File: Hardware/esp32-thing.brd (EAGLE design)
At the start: 25.4 x 58.9 mm, 72 parts, among them Q1 2.5A/30V, Q2 MBT3904DW1T1, U1 MCP73831, U2 ESP3212, U3 AP2112K-3.3V, U4 FT231XS, U5 W25Q32FVSS, Y1 26MHz, Y2 32.768kHz

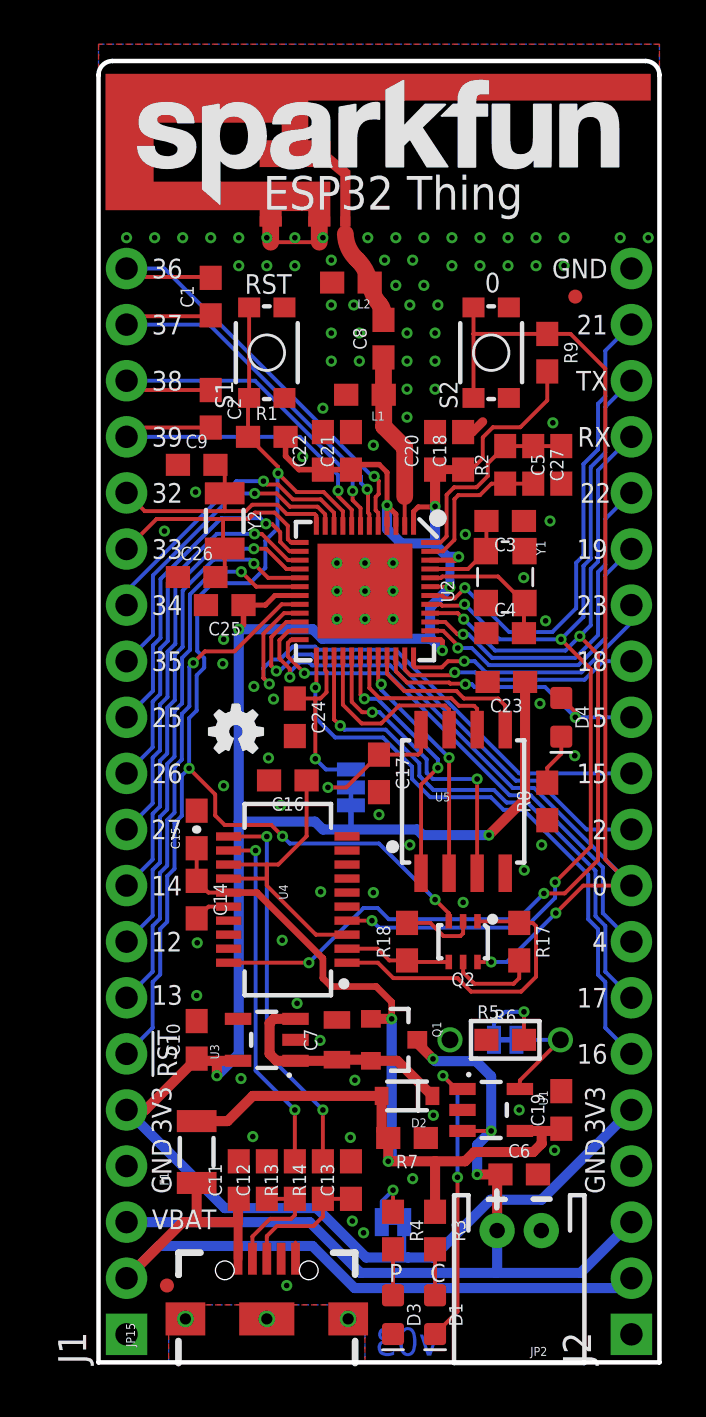
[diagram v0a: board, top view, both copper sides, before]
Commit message: Upping to v10, fixing some silk.
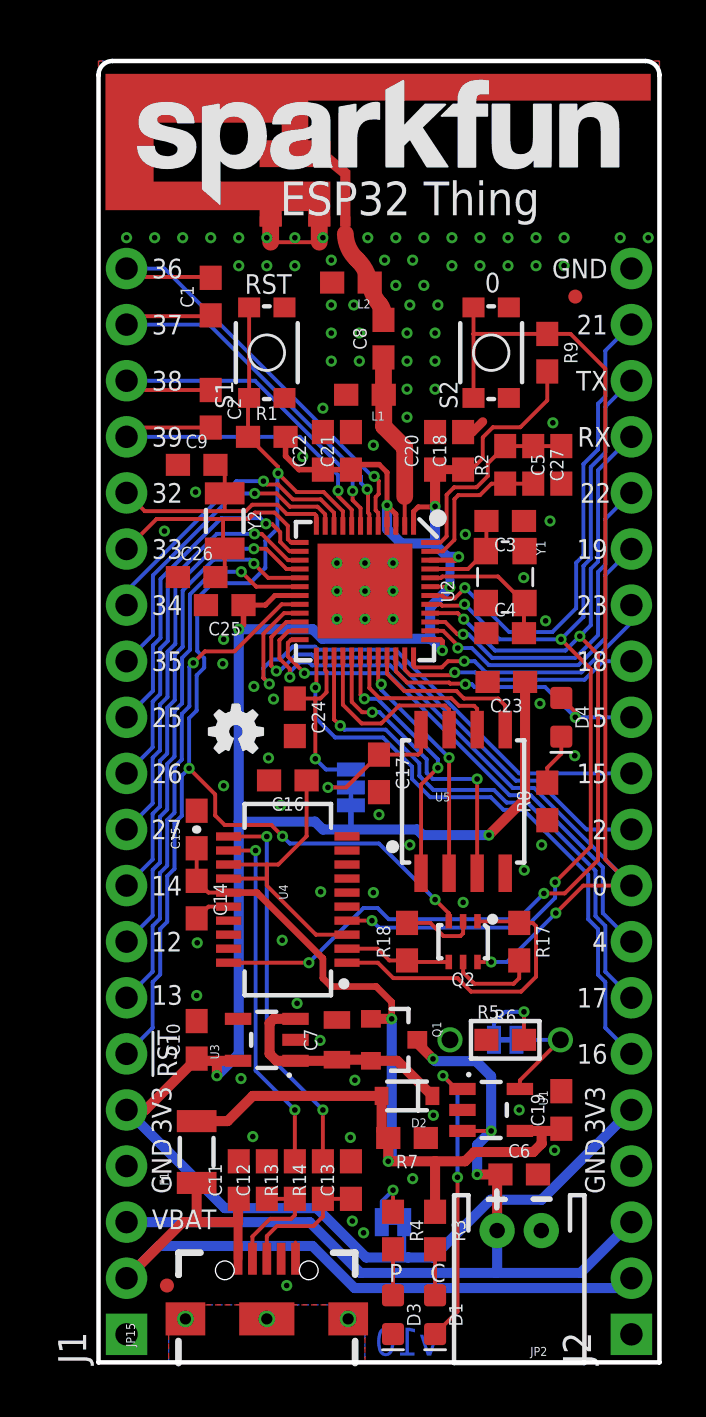
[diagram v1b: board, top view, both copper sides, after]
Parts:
- moved LOGO3 0.13 mm to (23.7, 53.1)
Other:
- board text added: "http://sfe.io/t5O7"
- board text added: "v10"
- board text removed: "http://sfe.io/t507"
- board text removed: "v03"
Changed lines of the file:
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@@
 <?xml version="1.0" encoding="utf-8"?>
 <!DOCTYPE eagle SYSTEM "eagle.dtd">
-<eagle version="7.6.0">
+<eagle version="7.5.0">
 <drawing>
 <settings>
@@
 <layer number="47" name="Measures" color="7" fill="1" visible="no" active="yes"/>
 <layer number="48" name="Document" color="7" fill="1" visible="no" active="yes"/>
-<layer number="49" name="Reference" color="7" fill="1" visible="no" active="yes"/>
+<layer number="49" name="Reference" color="7" fill="1" visible="yes" active="yes"/>
 <layer number="50" name="dxf" color="7" fill="1" visible="no" active="no"/>
 <layer number="51" name="tDocu" color="6" fill="1" visible="yes" active="yes"/>
@@
 <text x="17.8435" y="48.4505" size="0.889" layer="21" font="vector" ratio="15" align="bottom-center">0</text>
 <text x="22.9235" y="6.35" size="0.8128" layer="22" font="vector" ratio="15" rot="MR270" align="bottom-center">VBAT</text>
-<text x="13.335" y="53.721" size="1.524" layer="21" font="vector" ratio="15" align="top-center">ESP32 Thing</text>
+<text x="14.097" y="53.467" size="1.524" layer="21" font="vector" ratio="15" align="top-center">ESP32 Thing</text>
 <dimension x1="0" y1="0" x2="0" y2="58.928" x3="-5.08" y3="29.464" textsize="1.778" textratio="15" layer="47" dtype="vertical" width="0.127" unit="inch" precision="3"/>
 <dimension x1="0" y1="0" x2="25.4" y2="0" x3="12.7" y3="-7.62" textsize="1.778" textratio="15" layer="47" dtype="horizontal" width="0.127" unit="inch" precision="3"/>
@@
 PROG</text>
 <text x="12.573" y="26.162" size="0.8128" layer="22" font="vector" ratio="15" rot="MR270" align="top-center">SJ3</text>
-<text x="13.97" y="0.3048" size="1.27" layer="16" font="vector" ratio="15" rot="MR0" align="bottom-center">v03</text>
+<text x="13.97" y="0.3048" size="1.27" layer="16" font="vector" ratio="15" rot="MR0" align="bottom-center">v10</text>
 <text x="13.97" y="-19.05" size="1.778" layer="51" font="vector" ratio="15">Jim Lindblom</text>
 <text x="13.462" y="3.6449" size="0.8128" layer="21" font="vector" ratio="15" align="bottom-center">P</text>
 <text x="15.367" y="3.6449" size="0.8128" layer="21" font="vector" ratio="15" align="bottom-center">C</text>
-<text x="12.065" y="54.61" size="1.27" layer="22" font="vector" ratio="15" rot="MR0" align="top-center">ESP32 Thing</text>
+<text x="12.065" y="54.61" size="1.524" layer="22" font="vector" ratio="15" rot="MR0" align="top-center">ESP32 Thing</text>
 <wire x1="18.034" y1="6.9977" x2="18.034" y2="7.7597" width="0.254" layer="21"/>
 <wire x1="18.415" y1="7.3787" x2="17.653" y2="7.3787" width="0.254" layer="21"/>
@@
 <text x="11.43" y="27.686" size="0.8128" layer="22" font="vector" ratio="15" rot="MR90" align="center-left">FLASH
 VCC</text>
-<text x="12.065" y="52.07" size="1.27" layer="22" font="vector" ratio="15" rot="MR0" align="center">http://sfe.io/t507</text>
+<text x="12.446" y="51.816" size="1.397" layer="22" font="vector" ratio="15" rot="MR0" align="center">http://sfe.io/t5O7</text>
 <text x="2.413" y="41.91" size="0.889" layer="21" font="vector" ratio="15" align="center-left">39</text>
 <text x="2.413" y="44.45" size="0.889" layer="21" font="vector" ratio="15" align="center-left">38</text>
@@
 <element name="FD1" library="SparkFun-Aesthetics" package="MICRO-FIDUCIAL" value="FIDUCIALUFIDUCIAL" x="3.0988" y="3.4798"/>
 <element name="FD2" library="SparkFun-Aesthetics" package="MICRO-FIDUCIAL" value="FIDUCIALUFIDUCIAL" x="21.59" y="48.26"/>
-<element name="LOGO3" library="SparkFun-Aesthetics" package="SFE_LOGO_NAME_.2" value="SFE_LOGO_NAME.2_INCH" x="23.749" y="53.213" rot="MR0"/>
+<element name="LOGO3" library="SparkFun-Aesthetics" package="SFE_LOGO_NAME_.2" value="SFE_LOGO_NAME.2_INCH" x="23.749" y="53.086" rot="MR0"/>
 <element name="R9" library="SparkFun-Resistors" package="0603" value="10k" x="20.32" y="45.72" rot="R270">
 <attribute name="PROD_ID" value="RES-00824" x="20.32" y="45.72" size="1.778" layer="27" font="vector" ratio="15" rot="R270" display="off"/>
@@
 <contactref element="C25" pad="2"/>
 <polygon width="0.1778" layer="1" isolate="0.1778" rank="6">
-<vertex x="0" y="59.69"/>
+<vertex x="0" y="58.928"/>
 <vertex x="0" y="0"/>
 <vertex x="25.4" y="0"/>
-<vertex x="25.4" y="59.69"/>
+<vertex x="25.4" y="58.928"/>
 </polygon>
 <polygon width="0.1778" layer="16" isolate="0.1778" rank="6">
-<vertex x="25.4" y="59.69"/>
+<vertex x="25.4" y="58.928"/>
 <vertex x="25.4" y="0"/>
 <vertex x="0" y="0"/>
-<vertex x="0" y="59.69"/>
+<vertex x="0" y="58.928"/>
 </polygon>
 <contactref element="S1" pad="2"/>

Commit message: Fixing label, SJ3 silk, reinforcing connection on USB ground.
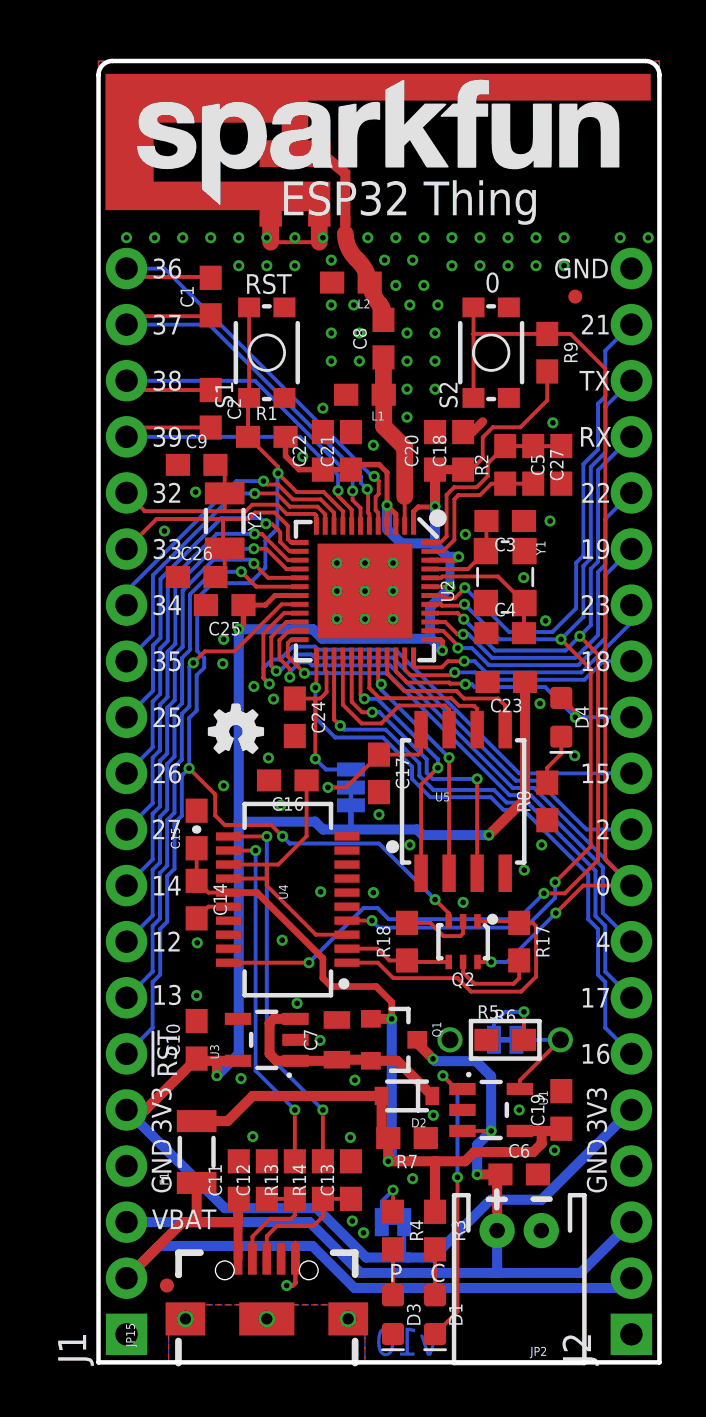
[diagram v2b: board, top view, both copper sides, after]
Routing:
- net GND: track 7.57 -> 9.15 mm
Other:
- board text added: "IC"
- board text added: "RXI"
- board text added: "TXO"
- board text removed: "SJ3"
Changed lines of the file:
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@@
 <text x="2.413" y="8.89" size="0.889" layer="21" font="vector" ratio="15" rot="R270" align="bottom-center">GND</text>
 <text x="2.413" y="6.477" size="0.889" layer="21" font="vector" ratio="15" align="center-left">VBAT</text>
-<text x="23.0505" y="36.83" size="0.889" layer="21" font="vector" ratio="15" align="center-right">19</text>
-<text x="23.0505" y="46.99" size="0.889" layer="21" font="vector" ratio="15" align="center-right">21</text>
-<text x="23.2029" y="39.37" size="0.889" layer="21" font="vector" ratio="15" align="center-right">22</text>
-<text x="23.2029" y="41.91" size="0.889" layer="21" font="vector" ratio="15" align="center-right">RX</text>
-<text x="23.0505" y="44.45" size="0.889" layer="21" font="vector" ratio="15" align="center-right">TX</text>
-<text x="23.0505" y="34.29" size="0.889" layer="21" font="vector" ratio="15" align="center-right">23</text>
-<text x="23.0505" y="31.75" size="0.889" layer="21" font="vector" ratio="15" align="center-right">18</text>
-<text x="23.0505" y="29.21" size="0.889" layer="21" font="vector" ratio="15" align="center-right">5</text>
-<text x="23.0505" y="26.67" size="0.889" layer="21" font="vector" ratio="15" align="center-right">15</text>
-<text x="23.0505" y="24.13" size="0.889" layer="21" font="vector" ratio="15" align="center-right">2</text>
-<text x="23.0505" y="21.59" size="0.889" layer="21" font="vector" ratio="15" align="center-right">0</text>
-<text x="23.0505" y="19.05" size="0.889" layer="21" font="vector" ratio="15" align="center-right">4</text>
-<text x="23.0505" y="16.51" size="0.889" layer="21" font="vector" ratio="15" align="center-right">17</text>
-<text x="23.0505" y="13.97" size="0.889" layer="21" font="vector" ratio="15" align="center-right">16</text>
-<text x="22.9235" y="11.43" size="0.889" layer="21" font="vector" ratio="15" rot="R90" align="bottom-center">3V3</text>
-<text x="22.9235" y="8.89" size="0.889" layer="21" font="vector" ratio="15" rot="R90" align="bottom-center">GND</text>
+<text x="23.2029" y="36.83" size="0.889" layer="21" font="vector" ratio="15" align="center-right">19</text>
+<text x="23.2029" y="46.99" size="0.889" layer="21" font="vector" ratio="15" align="center-right">21</text>
+<text x="23.2283" y="39.37" size="0.889" layer="21" font="vector" ratio="15" align="center-right">22</text>
+<text x="23.2537" y="41.91" size="0.889" layer="21" font="vector" ratio="15" align="center-right">RX</text>
+<text x="23.2029" y="44.45" size="0.889" layer="21" font="vector" ratio="15" align="center-right">TX</text>
+<text x="23.2029" y="34.29" size="0.889" layer="21" font="vector" ratio="15" align="center-right">23</text>
+<text x="23.2029" y="31.75" size="0.889" layer="21" font="vector" ratio="15" align="center-right">18</text>
+<text x="23.2029" y="29.21" size="0.889" layer="21" font="vector" ratio="15" align="center-right">5</text>
+<text x="23.2029" y="26.67" size="0.889" layer="21" font="vector" ratio="15" align="center-right">15</text>
+<text x="23.2029" y="24.13" size="0.889" layer="21" font="vector" ratio="15" align="center-right">2</text>
+<text x="23.2029" y="21.59" size="0.889" layer="21" font="vector" ratio="15" align="center-right">0</text>
+<text x="23.2029" y="19.05" size="0.889" layer="21" font="vector" ratio="15" align="center-right">4</text>
+<text x="23.2029" y="16.51" size="0.889" layer="21" font="vector" ratio="15" align="center-right">17</text>
+<text x="23.2029" y="13.97" size="0.889" layer="21" font="vector" ratio="15" align="center-right">16</text>
+<text x="23.0124" y="11.43" size="0.889" layer="21" font="vector" ratio="15" rot="R90" align="bottom-center">3V3</text>
+<text x="23.0124" y="8.89" size="0.889" layer="21" font="vector" ratio="15" rot="R90" align="bottom-center">GND</text>
 <text x="22.86" y="36.83" size="1.016" layer="22" font="vector" ratio="15" rot="MR0" align="center-left">19</text>
 <text x="22.86" y="46.99" size="1.016" layer="22" font="vector" ratio="15" rot="MR0" align="center-left">21</text>
 <text x="22.86" y="39.37" size="1.016" layer="22" font="vector" ratio="15" rot="MR0" align="center-left">22</text>
-<text x="22.86" y="41.91" size="1.016" layer="22" font="vector" ratio="15" rot="MR0" align="center-left">RX</text>
-<text x="22.86" y="44.45" size="1.016" layer="22" font="vector" ratio="15" rot="MR0" align="center-left">TX</text>
+<text x="22.86" y="41.91" size="1.016" layer="22" font="vector" ratio="15" rot="MR0" align="center-left">RXI</text>
+<text x="22.86" y="44.45" size="1.016" layer="22" font="vector" ratio="15" rot="MR0" align="center-left">TXO</text>
 <text x="22.86" y="34.29" size="1.016" layer="22" font="vector" ratio="15" rot="MR0" align="center-left">23</text>
 <text x="22.86" y="31.75" size="1.016" layer="22" font="vector" ratio="15" rot="MR0" align="center-left">18</text>
@@
 <text x="18.415" y="15.875" size="0.8128" layer="22" font="vector" ratio="15" rot="MR180" align="top-center">CHG
 PROG</text>
-<text x="12.573" y="26.162" size="0.8128" layer="22" font="vector" ratio="15" rot="MR270" align="top-center">SJ3</text>
+<text x="12.573" y="26.162" size="0.8128" layer="22" font="vector" ratio="15" rot="MR270" align="top-center">FLASH
+VCC</text>
 <text x="13.97" y="0.3048" size="1.27" layer="16" font="vector" ratio="15" rot="MR0" align="bottom-center">v10</text>
 <text x="13.97" y="-19.05" size="1.778" layer="51" font="vector" ratio="15">Jim Lindblom</text>
@@
 <wire x1="19.685" y1="7.3914" x2="20.447" y2="7.3914" width="0.254" layer="22"/>
 <text x="11.43" y="24.511" size="0.8128" layer="22" font="vector" ratio="15" rot="MR90" align="center-right">3V3</text>
-<text x="11.43" y="27.686" size="0.8128" layer="22" font="vector" ratio="15" rot="MR90" align="center-left">FLASH
-VCC</text>
+<text x="11.43" y="27.686" size="0.8128" layer="22" font="vector" ratio="15" rot="MR90" align="center-left">IC</text>
 <text x="12.446" y="51.816" size="1.397" layer="22" font="vector" ratio="15" rot="MR0" align="center">http://sfe.io/t5O7</text>
 <text x="2.413" y="41.91" size="0.889" layer="21" font="vector" ratio="15" align="center-left">39</text>
@@
 <text x="2.413" y="46.99" size="0.889" layer="21" font="vector" ratio="15" align="center-left">37</text>
 <text x="2.413" y="49.53" size="0.889" layer="21" font="vector" ratio="15" align="center-left">36</text>
-<text x="23.0505" y="49.53" size="0.889" layer="21" font="vector" ratio="15" align="center-right">GND</text>
+<text x="23.1267" y="49.53" size="0.889" layer="21" font="vector" ratio="15" align="center-right">GND</text>
 <text x="22.86" y="49.53" size="1.016" layer="22" font="vector" ratio="15" rot="MR0" align="center-left">GND</text>
 </plain>
@@
 <via x="7.9248" y="30.0355" extent="1-16" drill="0.254"/>
 <via x="16.6116" y="37.4904" extent="1-16" drill="0.254"/>
+<wire x1="8.5217" y1="3.4798" x2="8.8011" y2="3.4798" width="0.2032" layer="1"/>
+<wire x1="8.8011" y1="3.4798" x2="8.9154" y2="3.5941" width="0.2032" layer="1"/>
+<wire x1="8.9154" y1="3.5941" x2="8.9154" y2="4.7371" width="0.2032" layer="1"/>
 </signal>
 <signal name="LNA_IN">
